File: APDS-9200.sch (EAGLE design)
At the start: 12 parts

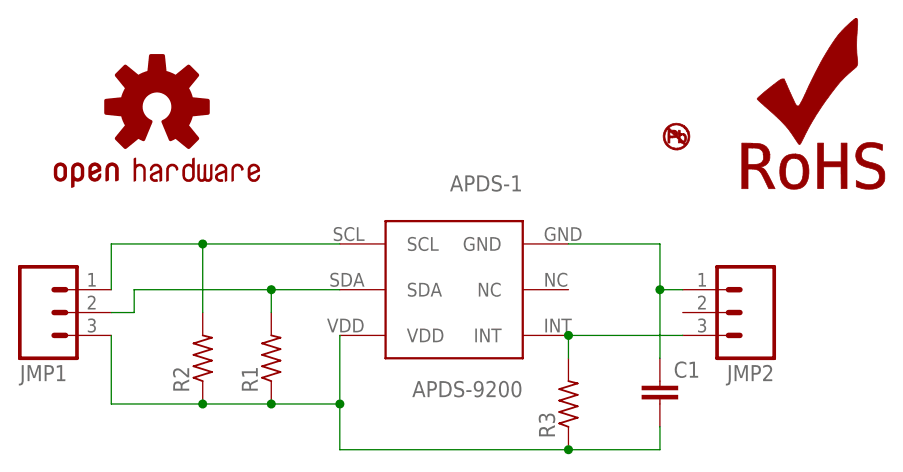
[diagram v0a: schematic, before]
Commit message: Fixed on board labels
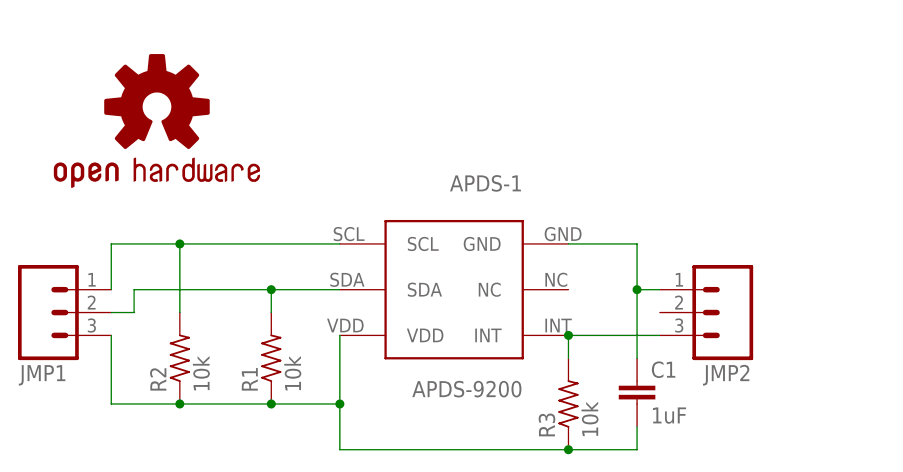
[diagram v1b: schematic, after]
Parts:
- removed LOGO2: NO_PB_LOGO, CalvEngIO-Logos:NO_PB_LOGO
- removed LOGO3: ROHS_LOGO, CalvEngIO-Logos:ROHS_LOGO
- removed U$2: WEBSITE.05, CalvEngIO-Logos:WEBSITE.05
- C1: value (none) -> 1uF
- R1, R2, R3: value (none) -> 10k
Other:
- moved on the sheet: C1, JMP2, R2
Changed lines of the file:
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@@
 <part name="JMP1" library="CalvEngIO-Connectors" deviceset="JMP-03" device=""/>
 <part name="JMP2" library="CalvEngIO-Connectors" deviceset="JMP-03" device=""/>
-<part name="C1" library="CalvEngIO-Passives" deviceset="CAPACITOR" device="0402"/>
-<part name="R1" library="CalvEngIO-Passives" deviceset="RESISTOR" device="0402"/>
-<part name="R2" library="CalvEngIO-Passives" deviceset="RESISTOR" device="0402"/>
-<part name="R3" library="CalvEngIO-Passives" deviceset="RESISTOR" device="0402"/>
+<part name="C1" library="CalvEngIO-Passives" deviceset="CAPACITOR" device="0402" value="1uF"/>
+<part name="R1" library="CalvEngIO-Passives" deviceset="RESISTOR" device="0402" value="10k"/>
+<part name="R2" library="CalvEngIO-Passives" deviceset="RESISTOR" device="0402" value="10k"/>
+<part name="R3" library="CalvEngIO-Passives" deviceset="RESISTOR" device="0402" value="10k"/>
 <part name="LOGO1" library="CalvEngIO-Logos" deviceset="OSHW-LOGO" device="MINI"/>
 <part name="U$1" library="CalvEngIO-Logos" deviceset="CALVENGIO_HANDLE" device="HANDLE.025"/>
-<part name="LOGO2" library="CalvEngIO-Logos" deviceset="NO_PB_LOGO" device=""/>
-<part name="LOGO3" library="CalvEngIO-Logos" deviceset="ROHS_LOGO" device=""/>
-<part name="U$2" library="CalvEngIO-Logos" deviceset="WEBSITE.05" device=""/>
 </parts>
 <sheets>
@@
 <attribute name="NAME" x="22.86" y="34.798" size="1.778" layer="95" rot="MR180"/>
 </instance>
-<instance part="JMP2" gate="G$1" x="101.6" y="40.64" smashed="yes" rot="R180">
-<attribute name="NAME" x="106.68" y="34.798" size="1.778" layer="95" rot="R180"/>
+<instance part="JMP2" gate="G$1" x="99.06" y="40.64" smashed="yes" rot="R180">
+<attribute name="NAME" x="104.14" y="34.798" size="1.778" layer="95" rot="R180"/>
 </instance>
-<instance part="C1" gate="G$1" x="93.98" y="30.48" smashed="yes">
-<attribute name="NAME" x="95.504" y="33.401" size="1.778" layer="95"/>
-<attribute name="VALUE" x="95.504" y="28.321" size="1.778" layer="96"/>
+<instance part="C1" gate="G$1" x="91.44" y="30.48" smashed="yes">
+<attribute name="NAME" x="92.964" y="33.401" size="1.778" layer="95"/>
+<attribute name="VALUE" x="92.964" y="28.321" size="1.778" layer="96"/>
 </instance>
 <instance part="R1" gate="G$1" x="50.8" y="35.56" smashed="yes" rot="R90">
@@
 <attribute name="VALUE" x="54.102" y="31.75" size="1.778" layer="96" rot="R90"/>
 </instance>
-<instance part="R2" gate="G$1" x="43.18" y="35.56" smashed="yes" rot="R90">
-<attribute name="NAME" x="41.6814" y="31.75" size="1.778" layer="95" rot="R90"/>
-<attribute name="VALUE" x="46.482" y="31.75" size="1.778" layer="96" rot="R90"/>
+<instance part="R2" gate="G$1" x="40.64" y="35.56" smashed="yes" rot="R90">
+<attribute name="NAME" x="39.1414" y="31.75" size="1.778" layer="95" rot="R90"/>
+<attribute name="VALUE" x="43.942" y="31.75" size="1.778" layer="96" rot="R90"/>
 </instance>
 <instance part="R3" gate="G$1" x="83.82" y="30.48" smashed="yes" rot="R90">
@@
 <instance part="LOGO1" gate="G$1" x="38.1" y="63.5"/>
 <instance part="U$1" gate="G$1" x="53.34" y="60.96"/>
-<instance part="LOGO2" gate="G$1" x="93.98" y="58.42"/>
-<instance part="LOGO3" gate="G$1" x="101.6" y="53.34"/>
-<instance part="U$2" gate="G$1" x="50.8" y="68.58"/>
 </instances>
 <busses>
@@
 <wire x1="58.42" y1="30.48" x2="50.8" y2="30.48" width="0.1524" layer="91"/>
 <pinref part="R2" gate="G$1" pin="1"/>
-<wire x1="50.8" y1="30.48" x2="43.18" y2="30.48" width="0.1524" layer="91"/>
+<wire x1="50.8" y1="30.48" x2="40.64" y2="30.48" width="0.1524" layer="91"/>
 <junction x="50.8" y="30.48"/>
 <wire x1="58.42" y1="30.48" x2="58.42" y2="25.4" width="0.1524" layer="91"/>
@@
 <wire x1="58.42" y1="25.4" x2="83.82" y2="25.4" width="0.1524" layer="91"/>
 <pinref part="C1" gate="G$1" pin="2"/>
-<wire x1="83.82" y1="25.4" x2="93.98" y2="25.4" width="0.1524" layer="91"/>
-<wire x1="93.98" y1="25.4" x2="93.98" y2="27.94" width="0.1524" layer="91"/>
+<wire x1="83.82" y1="25.4" x2="91.44" y2="25.4" width="0.1524" layer="91"/>
+<wire x1="91.44" y1="25.4" x2="91.44" y2="27.94" width="0.1524" layer="91"/>
 <junction x="83.82" y="25.4"/>
 <pinref part="JMP1" gate="G$1" pin="4"/>
 <wire x1="33.02" y1="38.1" x2="33.02" y2="30.48" width="0.1524" layer="91"/>
-<wire x1="33.02" y1="30.48" x2="43.18" y2="30.48" width="0.1524" layer="91"/>
-<junction x="43.18" y="30.48"/>
+<wire x1="33.02" y1="30.48" x2="40.64" y2="30.48" width="0.1524" layer="91"/>
+<junction x="40.64" y="30.48"/>
 </segment>
 </net>
@@
 <wire x1="83.82" y1="35.56" x2="83.82" y2="38.1" width="0.1524" layer="91"/>
 <pinref part="JMP2" gate="G$1" pin="4"/>
-<wire x1="83.82" y1="38.1" x2="96.52" y2="38.1" width="0.1524" layer="91"/>
+<wire x1="83.82" y1="38.1" x2="93.98" y2="38.1" width="0.1524" layer="91"/>
 <junction x="83.82" y="38.1"/>
 </segment>
@@
 <segment>
 <pinref part="R2" gate="G$1" pin="2"/>
-<wire x1="43.18" y1="40.64" x2="43.18" y2="48.26" width="0.1524" layer="91"/>
+<wire x1="40.64" y1="40.64" x2="40.64" y2="48.26" width="0.1524" layer="91"/>
 <pinref part="APDS-1" gate="G$1" pin="SCL"/>
-<wire x1="43.18" y1="48.26" x2="58.42" y2="48.26" width="0.1524" layer="91"/>
-<junction x="43.18" y="48.26"/>
+<wire x1="40.64" y1="48.26" x2="58.42" y2="48.26" width="0.1524" layer="91"/>
+<junction x="40.64" y="48.26"/>
 <pinref part="JMP1" gate="G$1" pin="2"/>
 <wire x1="33.02" y1="43.18" x2="33.02" y2="48.26" width="0.1524" layer="91"/>
-<wire x1="33.02" y1="48.26" x2="43.18" y2="48.26" width="0.1524" layer="91"/>
+<wire x1="33.02" y1="48.26" x2="40.64" y2="48.26" width="0.1524" layer="91"/>
 </segment>
 </net>
@@
 <segment>
 <pinref part="C1" gate="G$1" pin="1"/>
-<wire x1="93.98" y1="35.56" x2="93.98" y2="43.18" width="0.1524" layer="91"/>
+<wire x1="91.44" y1="35.56" x2="91.44" y2="43.18" width="0.1524" layer="91"/>
 <pinref part="JMP2" gate="G$1" pin="2"/>
-<wire x1="93.98" y1="43.18" x2="96.52" y2="43.18" width="0.1524" layer="91"/>
+<wire x1="91.44" y1="43.18" x2="93.98" y2="43.18" width="0.1524" layer="91"/>
 <pinref part="APDS-1" gate="G$1" pin="GND"/>
-<wire x1="83.82" y1="48.26" x2="93.98" y2="48.26" width="0.1524" layer="91"/>
-<wire x1="93.98" y1="48.26" x2="93.98" y2="43.18" width="0.1524" layer="91"/>
-<junction x="93.98" y="43.18"/>
+<wire x1="83.82" y1="48.26" x2="91.44" y2="48.26" width="0.1524" layer="91"/>
+<wire x1="91.44" y1="48.26" x2="91.44" y2="43.18" width="0.1524" layer="91"/>
+<junction x="91.44" y="43.18"/>
 </segment>
 </net>
